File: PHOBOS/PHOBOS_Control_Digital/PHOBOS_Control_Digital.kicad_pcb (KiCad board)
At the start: 4 copper layers, 35.6 x 58.4 mm, 69 parts, among them J12 PWR, J14 PS1-2, J15 PS3-4, J2 RF_OUT, J3 USB4056-03-A_REVA2, J4 Screw_Terminal_01x02, J8 Conn_01x02, U1 SX1280IMLTRT, U2 W25Q128JVSIQ, U3 NCP1117-3.3_SOT223, U4 RP2040, U5 TPS60403DBV, Y1 C1E-52.000-10-1012-X-M, Y2 ABM8-272-T3

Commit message: Schematic cleaned up for review.
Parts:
- J8: value Conn_01x02 -> BOOT
- TP11: value GPIO22 -> GPIO19
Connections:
- U4 pad 26: /RUN -> unconnected-(U4-RUN-Pad26)
- U4 pad 35: Net-(U4-GPIO23) -> unconnected-(U4-GPIO23-Pad35)
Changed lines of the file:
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@@
 		(capping no)
 		(filling no)
-		(zone_defaults)
 		(grid_origin 158.088005 135.374499)
 		(pcbplotparams
@@
 				(name "A")
 				(pins "3" "16" "17" "18" "19" "4" "6" "1" "11" "15" "2" "12" "14" "7"
-					"8" "9" "10" "22" "25" "20" "21" "13" "23" "24" "5"
+					"8" "9" "10" "22" "25" "5" "13" "20" "21" "23" "24"
 				)
 			)
@@
 			(layers "F.Cu" "F.Mask" "F.Paste")
 			(roundrect_rratio 0.25)
-			(net "/RUN")
+			(net "unconnected-(U4-RUN-Pad26)")
 			(pinfunction "RUN_26")
-			(pintype "input")
+			(pintype "input+no_connect")
 		)
 		(pad "27" smd roundrect
@@
 			(net "unconnected-(U4-GPIO22-Pad34)")
 			(pinfunction "GPIO22_34")
-			(pintype "bidirectional")
+			(pintype "bidirectional+no_connect")
 		)
 		(pad "35" smd roundrect
@@
 			(layers "F.Cu" "F.Mask" "F.Paste")
 			(roundrect_rratio 0.25)
-			(net "Net-(U4-GPIO23)")
+			(net "unconnected-(U4-GPIO23-Pad35)")
 			(pinfunction "GPIO23_35")
-			(pintype "bidirectional")
+			(pintype "bidirectional+no_connect")
 		)
 		(pad "36" smd roundrect
@@
 			)
 		)
-		(property "KiLib_Generator" "SMD_2terminal_chip_molded"
-			(at 0 0 90)
-			(layer "F.SilkS")
-			(hide yes)
-			(effects
-				(font
-					(size 1 1)
-					(thickness 0.15)
-				)
-			)
-		)
 		(property "Link" "https://www.digikey.com/en/products/detail/yageo/AC0402FR-7W4K7L/17009027"
 			(at 0 0 90)
@@
 			)
 		)
-		(property "Value" "Conn_01x02"
+		(property "Value" "BOOT"
 			(at 0 4.92 0)
 			(layer "F.Fab")
@@
 			)
 		)
-		(attr through_hole)
+		(attr through_hole exclude_from_bom)
 		(duplicate_pad_numbers_are_jumpers no)
 		(fp_line
@@
 			)
 		)
-		(property "KiLib_Generator" "SMD_2terminal_chip_molded"
-			(at 0 0 90)
-			(layer "F.SilkS")
-			(hide yes)
-			(effects
-				(font
-					(size 1 1)
-					(thickness 0.15)
-				)
-			)
-		)
 		(property "Link" "https://www.digikey.com/en/products/detail/yageo/AC0402FR-7W4K7L/17009027"
 			(at 0 0 270)
@@
 			)
 		)
-		(property "Value" "GPIO22"
+		(property "Value" "GPIO19"
 			(at 0 -2.05 0)
 			(layer "B.SilkS")

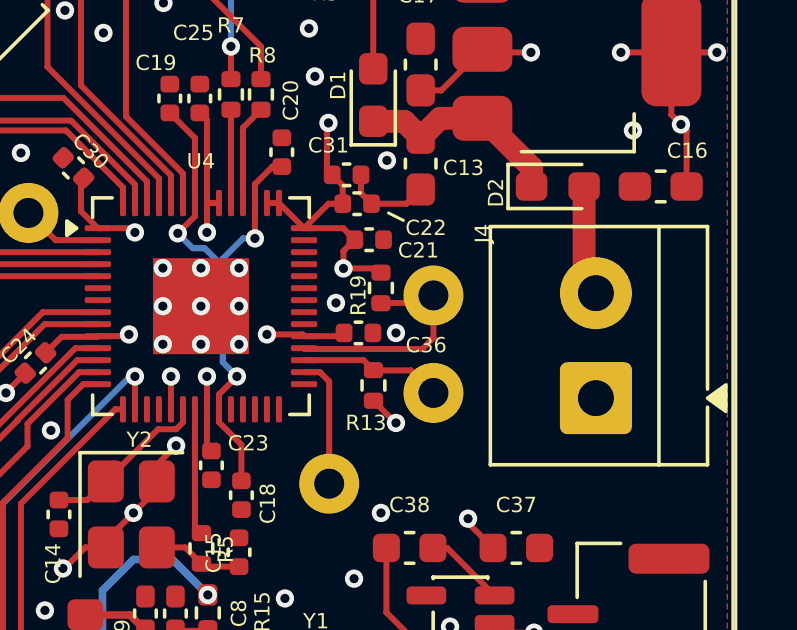
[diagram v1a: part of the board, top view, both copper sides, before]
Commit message: Batt measure added
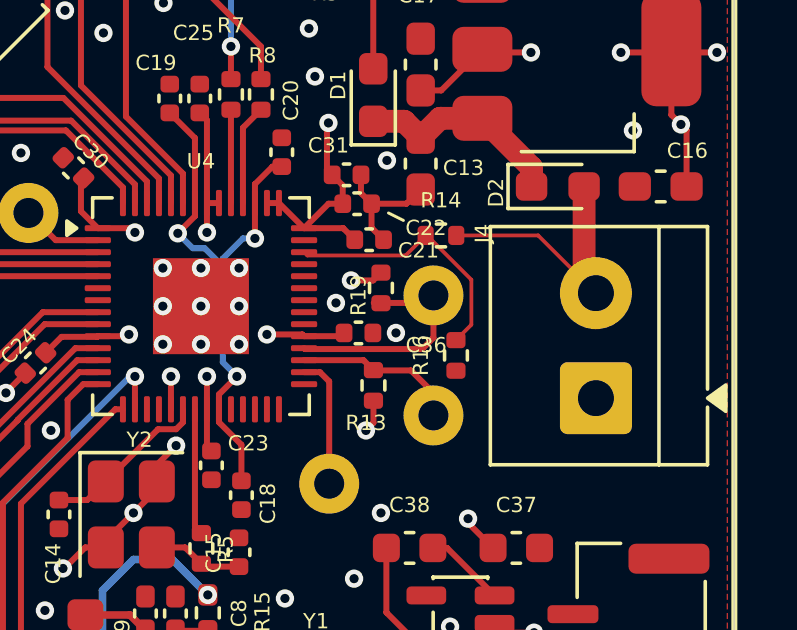
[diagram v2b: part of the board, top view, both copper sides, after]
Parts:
- added R14: 330k, Resistor_SMD:R_0402_1005Metric, F.Cu at (166.1, 96.9)
- added R16: 100K, Resistor_SMD:R_0402_1005Metric, F.Cu at (166.6, 100.9)
- moved TP7 0.75 mm to (165.8, 102.9)
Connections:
- U4 pad 40: unconnected-(U4-GPIO28_ADC2-Pad40) -> /BATT_CONT
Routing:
- net /BATT_CONT: track 0.00 -> 8.74 mm
- net +BATT: track 3.72 -> 9.17 mm
- net GND: track 15.2 -> 16.6 mm
- net +3V3: track 62.3 -> 61.3 mm
- net /SDA: track 4.76 -> 5.51 mm

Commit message: BOM Updated
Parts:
- moved R14 0.25 mm to (166.1, 97.1)
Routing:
- net /MOSI: track 29.6 -> 30.3 mm

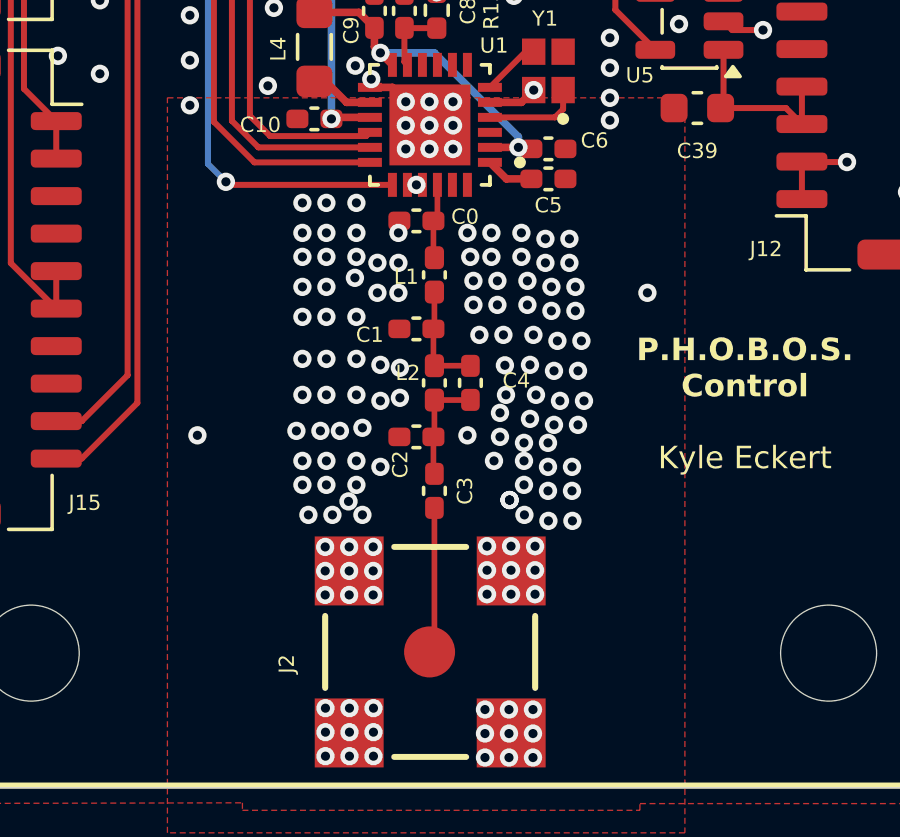
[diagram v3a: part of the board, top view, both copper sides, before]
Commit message: stackup and impedance matching adjusted for PCBway Guidelines
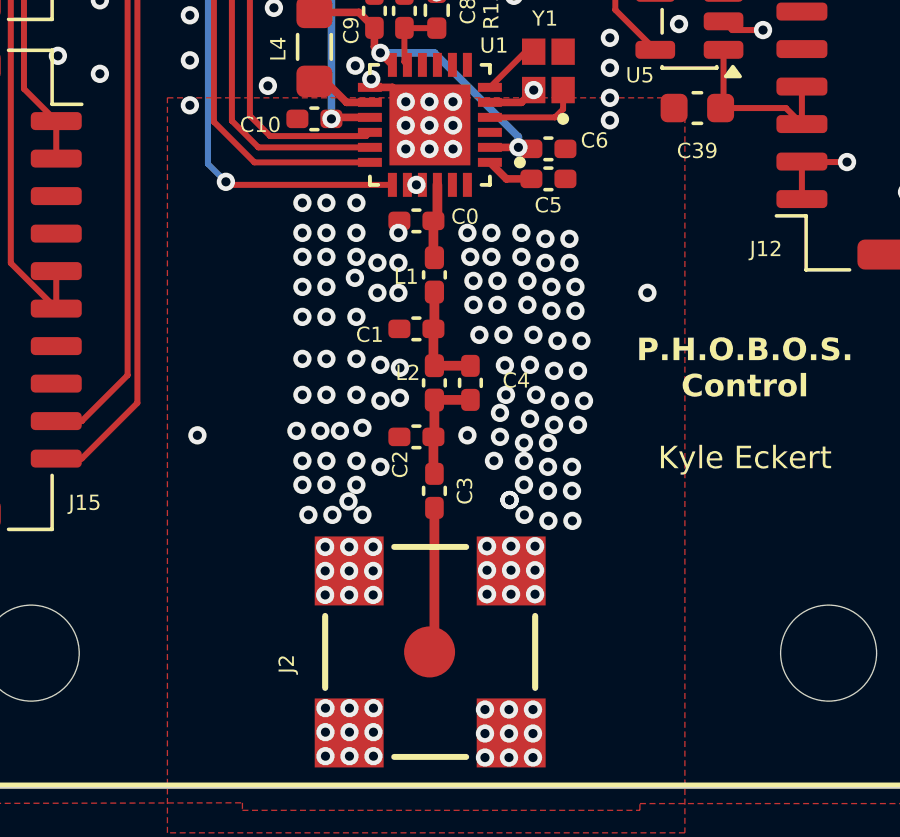
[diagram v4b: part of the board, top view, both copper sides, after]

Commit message: review submission files created
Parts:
- J4: value Screw_Terminal_01x02 -> BATT
- moved H4 47.6 mm to (184.3, 85.1), turned to 90 degrees
- moved H2 43.9 mm to (184.3, 111.7), turned to 90 degrees
- moved J2 41.7 mm to (184.3, 98.4), turned to 180 degrees
- moved H1 36.7 mm to (134.9, 85.1), turned to 90 degrees
- moved C3 34.2 mm to (178.9, 98.2), turned to 0 degrees
- moved D3 33.8 mm to (139.5, 83.2), turned to -90 degrees
- moved J3 32.3 mm to (132.3, 98.4), turned to -90 degrees
- moved H3 31.8 mm to (134.9, 111.7), turned to 90 degrees
- moved C2 31.5 mm to (177.1, 98.8), turned to -90 degrees
- moved R4 30.6 mm to (139.9, 86.0), turned to -90 degrees
- moved C4 29.5 mm to (175.3, 97.0), turned to 0 degrees
- moved J12 29.2 mm to (166.0, 84.1), turned to 180 degrees
- moved L2 29.1 mm to (175.3, 98.2), turned to 0 degrees
- moved J15 29.0 mm to (172.2, 112.7), turned to 0 degrees
- moved C16 27.6 mm to (148.7, 83.1), turned to -90 degrees
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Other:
- board size 35.6 x 58.4 mm -> 58.4 x 35.6 mm
- board text removed: "Kyle Eckert"

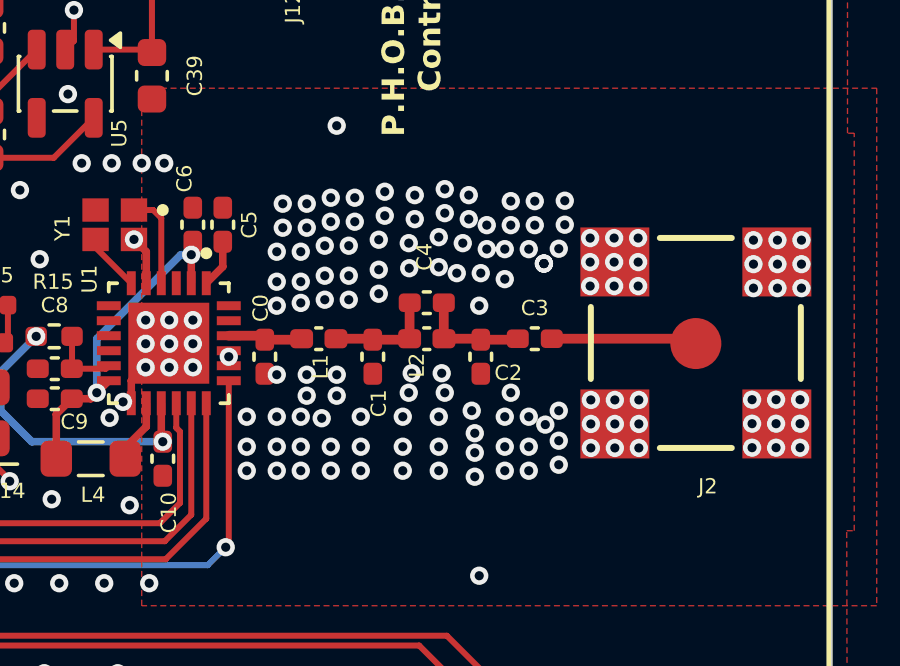
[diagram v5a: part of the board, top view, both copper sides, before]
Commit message: Via Ocean Removed
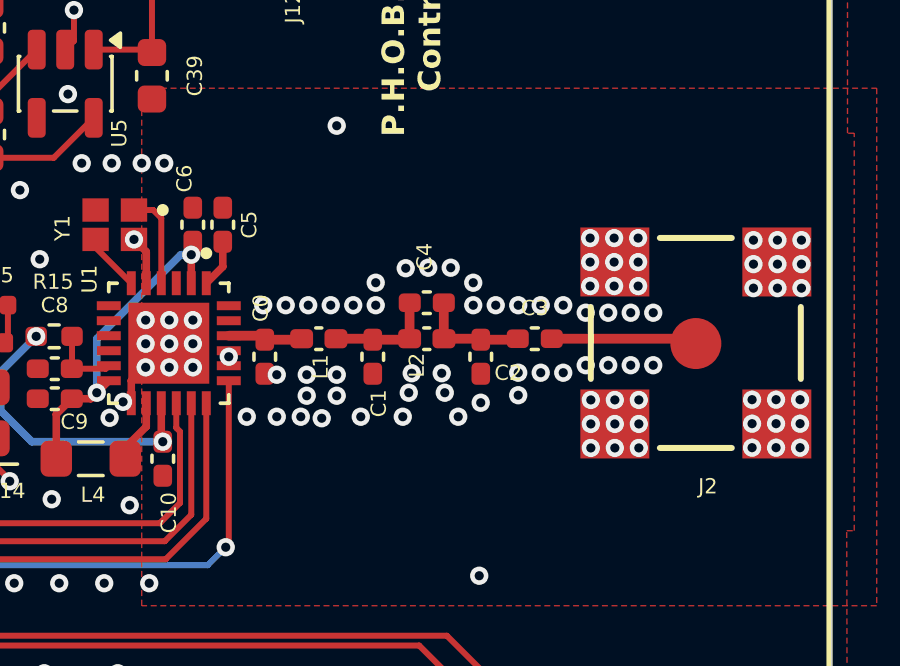
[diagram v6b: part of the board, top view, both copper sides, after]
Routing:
- net GND: vias 212 -> 159
